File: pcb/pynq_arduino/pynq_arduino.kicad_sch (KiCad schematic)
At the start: 3 parts, among them J1 Conn_02x11_Odd_Even, J2 Conn_01x15_Pin

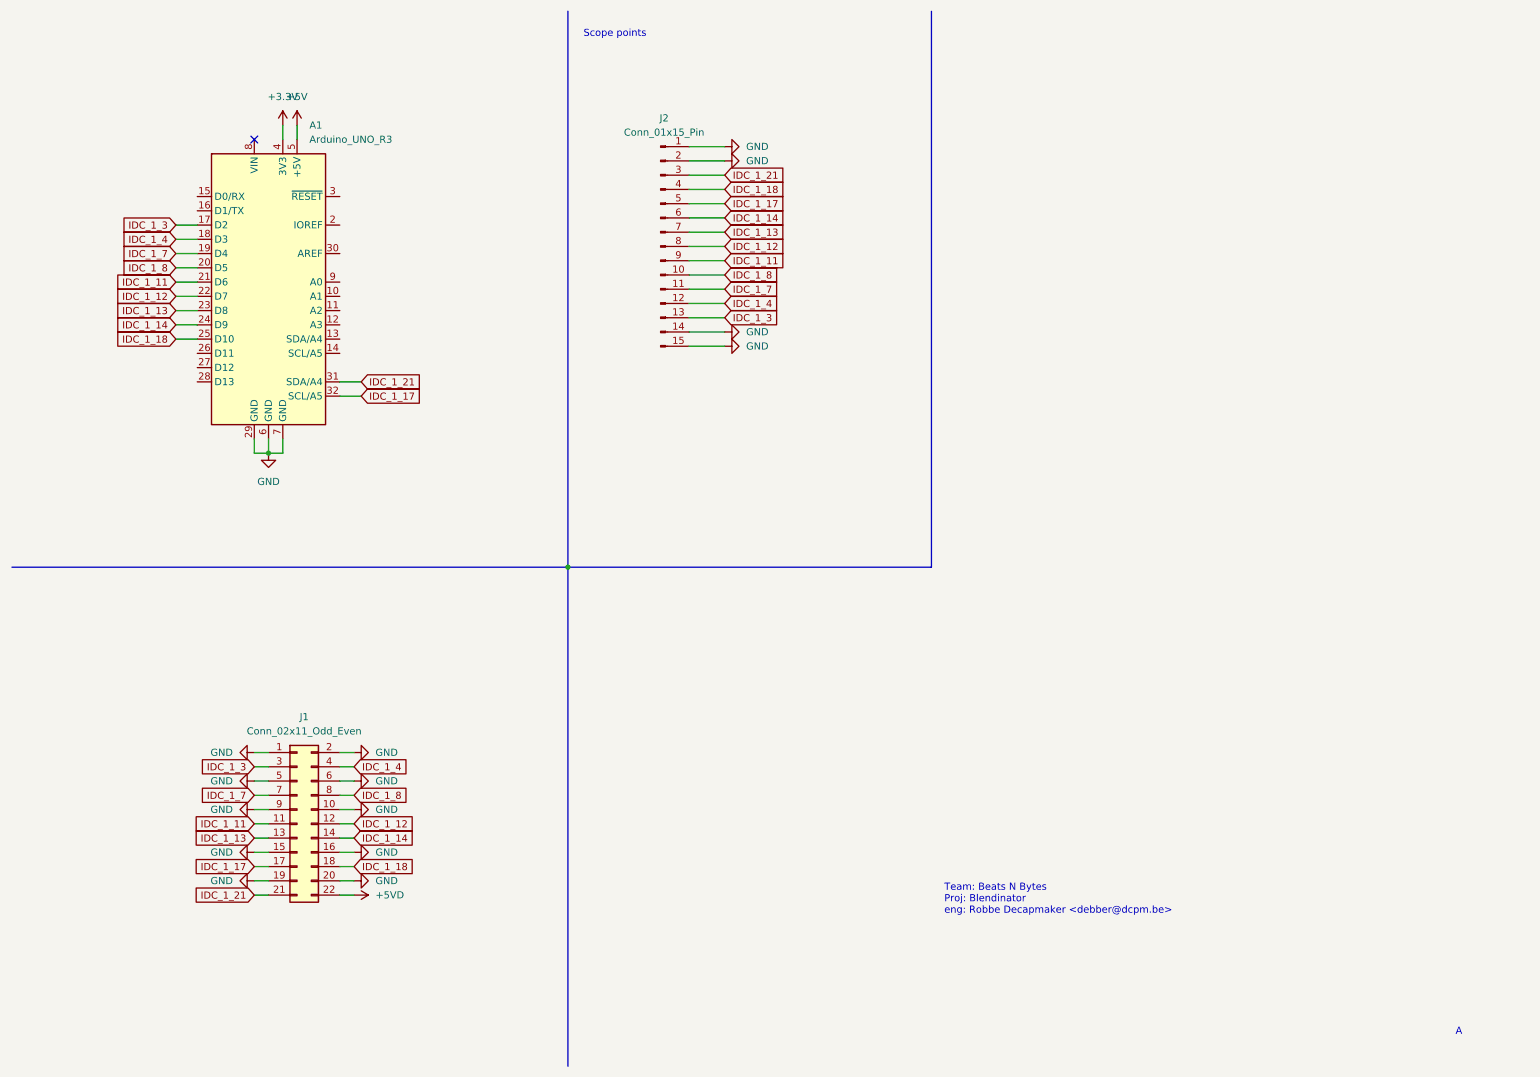
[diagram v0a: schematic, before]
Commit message: Updating pynq pcb to have level shifters
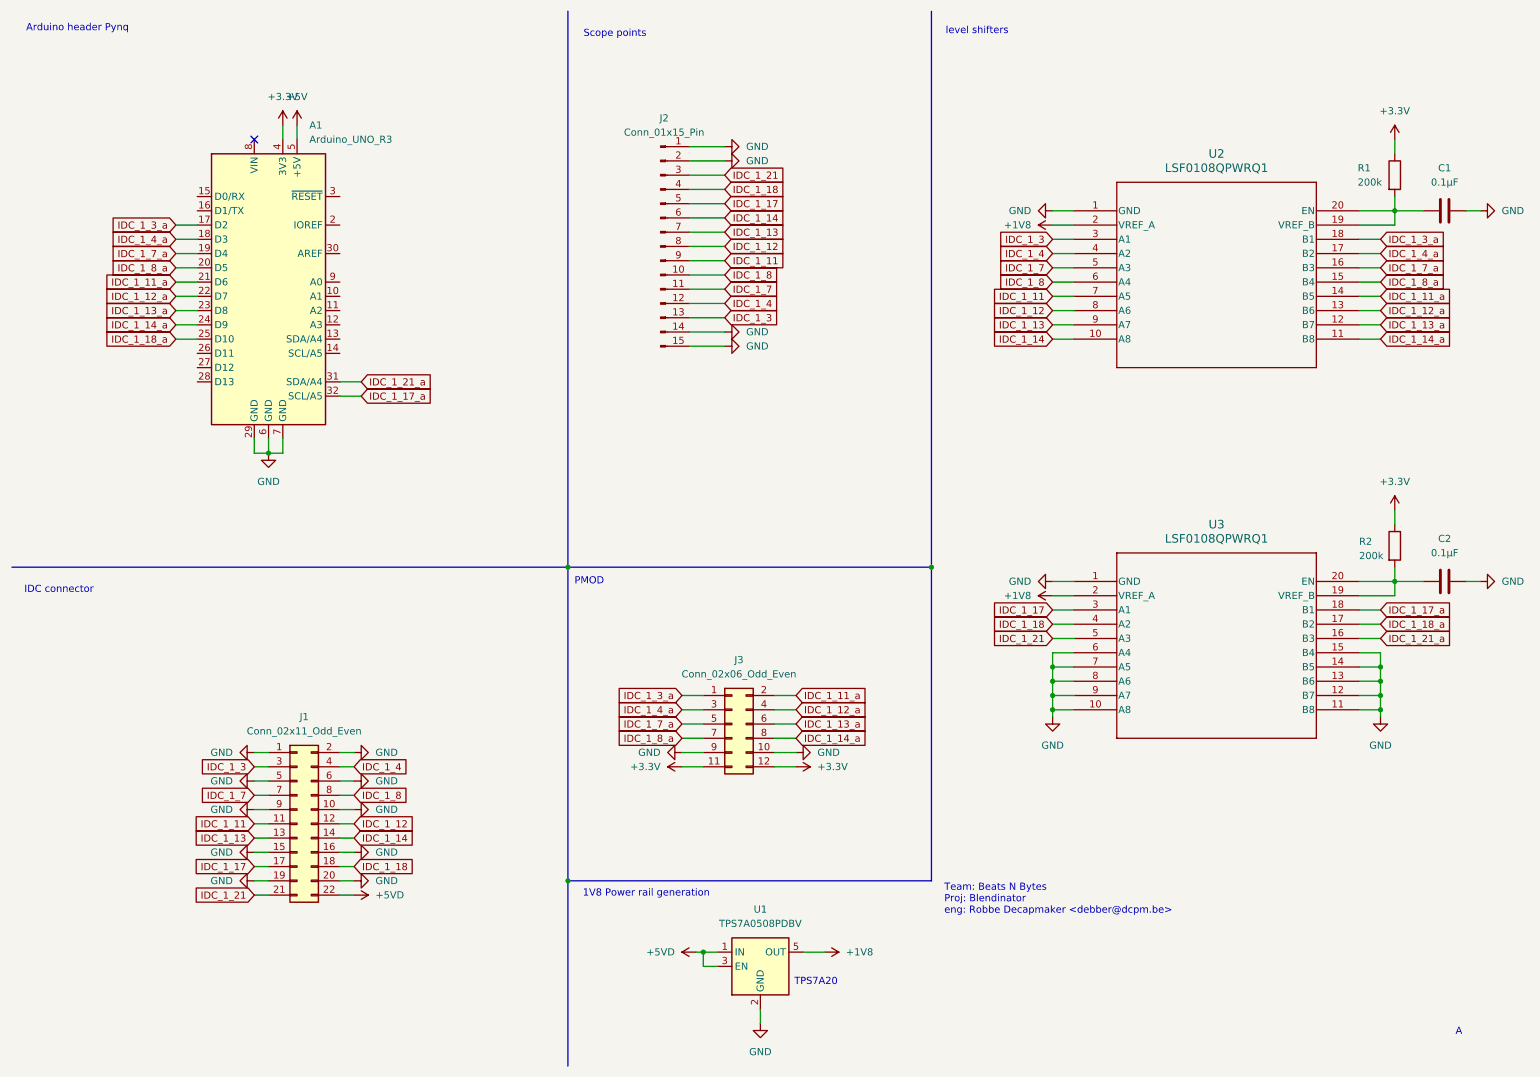
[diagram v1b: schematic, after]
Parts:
- added C1, C2: 0.1µF, Capacitor_SMD:C_0805_2012Metric_Pad1.18x1.45mm_HandSolder, symbol Device:C
- added J3: Conn_02x06_Odd_Even, Connector_PinHeader_2.54mm:PinHeader_2x06_P2.54mm_Horizontal, symbol Connector_Generic:Conn_02x06_Odd_Even
- added R1, R2: 200k, Resistor_SMD:R_0805_2012Metric_Pad1.20x1.40mm_HandSolder, symbol Device:R
- added U1: TPS7A0508PDBV, Package_TO_SOT_SMD:SOT-23-5, symbol Regulator_Linear:TPS7A0508PDBV
- added U2, U3: LSF0108QPWRQ1, level_shifter:PW20_TEX, symbol level_shifter:LSF0108QPWRQ1
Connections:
- net +3.3V: now also J3.11 (Pin_11), J3.12 (Pin_12), R1.1, R2.1
- net +5VD: now also U1.1 (IN), U1.3 (EN)
- net GND: now also C1.1, C2.1, J3.10 (Pin_10), J3.9 (Pin_9), U1.2 (GND), U2.1 (GND), U3.1 (GND), U3.10 (A8), U3.11 (B8), U3.12 (B7), U3.13 (B6), U3.14 (B5), U3.15 (B4), U3.6 (A4), U3.7 (A5), U3.8 (A6), U3.9 (A7)
- net IDC_1_11: now also U2.7 (A5); no longer A1.21 (D6)
- net IDC_1_12: now also U2.8 (A6); no longer A1.22 (D7)
- net IDC_1_13: now also U2.9 (A7); no longer A1.23 (D8)
- net IDC_1_14: now also U2.10 (A8); no longer A1.24 (D9)
- net IDC_1_17: now also U3.3 (A1); no longer A1.32 (SCL/A5)
- net IDC_1_18: now also U3.4 (A2); no longer A1.25 (D10)
- net IDC_1_21: now also U3.5 (A3); no longer A1.31 (SDA/A4)
- net IDC_1_3: now also U2.3 (A1); no longer A1.17 (D2)
- net IDC_1_4: now also U2.4 (A2); no longer A1.18 (D3)
- net IDC_1_7: now also U2.5 (A3); no longer A1.19 (D4)
- net IDC_1_8: now also U2.6 (A4); no longer A1.20 (D5)
- new net: C2.2, R2.2, U3.19 (VREF_B), U3.20 (EN)
- new net: C1.2, R1.2, U2.19 (VREF_B), U2.20 (EN)
- new net +1V8: U1.5 (OUT), U2.2 (VREF_A), U3.2 (VREF_A)
- new net IDC_1_11_a: A1.21 (D6), J3.2 (Pin_2), U2.14 (B5)
- new net IDC_1_12_a: A1.22 (D7), J3.4 (Pin_4), U2.13 (B6)
- new net IDC_1_13_a: A1.23 (D8), J3.6 (Pin_6), U2.12 (B7)
- new net IDC_1_14_a: A1.24 (D9), J3.8 (Pin_8), U2.11 (B8)
- new net IDC_1_17_a: A1.32 (SCL/A5), U3.18 (B1)
- new net IDC_1_18_a: A1.25 (D10), U3.17 (B2)
- new net IDC_1_21_a: A1.31 (SDA/A4), U3.16 (B3)
- new net IDC_1_3_a: A1.17 (D2), J3.1 (Pin_1), U2.18 (B1)
- new net IDC_1_4_a: A1.18 (D3), J3.3 (Pin_3), U2.17 (B2)
- new net IDC_1_7_a: A1.19 (D4), J3.5 (Pin_5), U2.16 (B3)
- new net IDC_1_8_a: A1.20 (D5), J3.7 (Pin_7), U2.15 (B4)
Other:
- note added: "1V8 Power rail generation"
- note added: "Arduino header Pynq"
- note added: "IDC connector"
- note added: "PMOD"
- note added: "TPS7A20"
- note added: "level shifters"
